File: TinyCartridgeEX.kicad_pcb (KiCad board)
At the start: 2 copper layers, 61.5 x 84.3 mm, 21 parts, among them U1 SN74AVC8T245PW, U2 SN74AVC8T245PW, U3 SN74AVC8T245PW, U4 74AHCV17A, U5 74LVC06A, U6 74LVC1G06, U7 74LVC3G17, U8 74LVC2G132, U9 TinyFPGA_EX, X1 EXPANSION_PORT_C64_EDGE

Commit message: Remove superfluous Schmitt buffers on NAND inputs
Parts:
- removed U8: 74LVC2G132, Package_SO:VSSOP-8_2.4x2.1mm_P0.5mm
- U7: value 74LVC3G17 -> 74LVC2G132; footprint Package_SO:TSSOP-8_3x3mm_P0.65mm -> Package_SO:VSSOP-8_2.4x2.1mm_P0.5mm
- moved U7 5.34 mm to (64.0, 136.4), turned to 0 degrees
- moved R4 4.21 mm to (47.0, 130.7)
- moved R5 4.21 mm to (48.3, 130.7)
- moved R6 4.21 mm to (49.5, 130.7)
- moved R7 4.21 mm to (50.8, 130.7)
- moved R8 4.21 mm to (52.1, 130.7)
- moved R9 4.21 mm to (53.3, 130.7)
- moved C1 3.00 mm to (51.3, 148.5), turned to 180 degrees
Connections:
- U4 pad 10: ~IO2 -> PHI2
- U4 pad 12: ~ROML -> DOTCLK
- U4 pad 3: Net-(U4-Pad3) -> (no net)
- U4 pad 4: PHI2 -> (no net)
- U4 pad 6: ~ROMH -> RESET_IN
- U4 pad 8: ~IO1 -> RW_IN
- U5 pad 2: Net-(U5-Pad2) -> Net-(U4-Pad9)
- U5 pad 6: Net-(U5-Pad6) -> Net-(U4-Pad5)
- U7 pad 1: Net-(U5-Pad2) -> Net-(U7-Pad1)
- U7 pad 2: RESET_IN -> Net-(U7-Pad2)
- U7 pad 3: Net-(U7-Pad3) -> IO12
- U7 pad 5: DOTCLK -> Net-(U7-Pad5)
- U7 pad 6: Net-(U5-Pad6) -> Net-(U7-Pad6)
- U7 pad 7: RW_IN -> ROMLH
- U9 pad 19: PHI2 -> BA
- U9 pad 20: Net-(U8-Pad7) -> IO12
- U9 pad 21: RW_IN -> PHI2
- U9 pad 28: RESET_IN -> RW_IN
- U9 pad 30: Net-(U8-Pad3) -> RESET_IN
- U9 pad 31: BA -> ROMLH
- X1 pad 10: Net-(U4-Pad11) -> Net-(U7-Pad6)
- X1 pad 11: Net-(U4-Pad13) -> Net-(U7-Pad1)
- X1 pad 5: Net-(U5-Pad2) -> Net-(U4-Pad9)
- X1 pad 6: Net-(U7-Pad3) -> Net-(U4-Pad13)
- X1 pad 7: Net-(U4-Pad9) -> Net-(U7-Pad5)
- X1 pad B: Net-(U4-Pad5) -> Net-(U7-Pad2)
- X1 pad C: Net-(U5-Pad6) -> Net-(U4-Pad5)
- X1 pad E: Net-(U4-Pad3) -> Net-(U4-Pad11)
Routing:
- net IO12: track 0.00 -> 43.1 mm
- net Net-(U8-Pad7): track 37.2 -> 0.00 mm
- net Net-(U7-Pad1): track 0.00 -> 35.8 mm, vias 0 -> 2
- net Net-(U7-Pad2): track 0.00 -> 33.5 mm, vias 0 -> 1
- net Net-(U5-Pad6): track 33.2 -> 0.00 mm, vias 3 -> 0
- net Net-(U5-Pad2): track 28.0 -> 0.00 mm
- net ROMLH: track 0.00 -> 27.7 mm
- net Net-(U7-Pad6): track 0.00 -> 26.9 mm
- net Net-(U7-Pad3): track 25.2 -> 0.00 mm
- net Net-(U7-Pad5): track 0.00 -> 25.0 mm
- net Net-(U4-Pad3): track 24.0 -> 0.00 mm, vias 1 -> 0
- net Net-(U8-Pad3): track 22.5 -> 0.00 mm
- net ~ROML: track 21.5 -> 0.00 mm, vias 1 -> 0
- net ~IO1: track 17.7 -> 0.00 mm, vias 1 -> 0
- net ~IO2: track 17.6 -> 0.00 mm, vias 1 -> 0
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
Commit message: Set correct logic families and add Mouser part# and pricing for BOM
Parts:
- U1, U2, U3: value SN74AVC8T245PW -> SN74LVC8T245
- U4: value 74AHCV17A -> 74LV17A
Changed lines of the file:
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@@
       (effects (font (size 1 1) (thickness 0.15)))
     )
-    (fp_text value 74AHCV17A (at 0 3.55 90) (layer F.Fab)
+    (fp_text value 74LV17A (at 0 3.55 90) (layer F.Fab)
       (effects (font (size 1 1) (thickness 0.15)))
     )
@@
       (effects (font (size 1 1) (thickness 0.15)))
     )
-    (fp_text value SN74AVC8T245PW (at 0 4.95 90) (layer F.Fab)
+    (fp_text value SN74LVC8T245 (at 0 4.95 90) (layer F.Fab)
       (effects (font (size 1 1) (thickness 0.15)))
     )
@@
       (effects (font (size 1 1) (thickness 0.15)))
     )
-    (fp_text value SN74AVC8T245PW (at 0 4.95 90) (layer F.Fab)
+    (fp_text value SN74LVC8T245 (at 0 4.95 90) (layer F.Fab)
       (effects (font (size 1 1) (thickness 0.15)))
     )
@@
       (effects (font (size 1 1) (thickness 0.15)))
     )
-    (fp_text value SN74AVC8T245PW (at 0 4.95 90) (layer F.Fab)
+    (fp_text value SN74LVC8T245 (at 0 4.95 90) (layer F.Fab)
       (effects (font (size 1 1) (thickness 0.15)))
     )
@@
   (segment (start 59.055 134.112) (end 55.88 130.937) (width 0.25) (layer F.Cu) (net 42))
   (segment (start 55.88 130.937) (end 55.88 108.839) (width 0.25) (layer F.Cu) (net 42))
+  (segment (start 77.47 153.543) (end 77.47 160.3248) (width 0.25) (layer F.Cu) (net 43))
+  (segment (start 70.428468 149.733) (end 73.66 149.733) (width 0.25) (layer F.Cu) (net 43))
+  (segment (start 73.66 149.733) (end 77.47 153.543) (width 0.25) (layer F.Cu) (net 43))
+  (segment (start 70.428468 149.733) (end 69.469 148.773532) (width 0.25) (layer F.Cu) (net 43))
+  (segment (start 65.958 140.306) (end 65.958 141.814) (width 0.25) (layer F.Cu) (net 43))
+  (via (at 65.958 141.814) (size 0.8) (drill 0.4) (layers F.Cu B.Cu) (net 43))
+  (via (at 69.469 143.764) (size 0.8) (drill 0.4) (layers F.Cu B.Cu) (net 43))
+  (segment (start 69.469 148.773532) (end 69.469 143.764) (width 0.25) (layer F.Cu) (net 43))
+  (segment (start 69.469 143.764) (end 69.469 142.494) (width 0.25) (layer B.Cu) (net 43))
+  (segment (start 68.789 141.814) (end 65.958 141.814) (width 0.25) (layer B.Cu) (net 43))
+  (segment (start 69.469 142.494) (end 68.789 141.814) (width 0.25) (layer B.Cu) (net 43))
+  (segment (start 57.15 151.384) (end 57.15 160.3248) (width 0.25) (layer B.Cu) (net 44))
+  (segment (start 57.15 151.384) (end 57.15 151.257) (width 0.25) (layer B.Cu) (net 44))
+  (segment (start 57.15 151.257) (end 56.388 150.495) (width 0.25) (layer B.Cu) (net 44))
+  (segment (start 56.388 150.495) (end 56.388 143.764) (width 0.25) (layer B.Cu) (net 44))
+  (via (at 56.388 143.764) (size 0.8) (drill 0.4) (layers F.Cu B.Cu) (net 44))
+  (segment (start 55.372 140.306) (end 55.372 141.605) (width 0.25) (layer F.Cu) (net 44))
+  (segment (start 56.388 142.621) (end 56.388 143.764) (width 0.25) (layer F.Cu) (net 44))
+  (segment (start 55.372 141.605) (end 56.388 142.621) (width 0.25) (layer F.Cu) (net 44))
   (segment (start 79.502 134.79) (end 79.502 132.588) (width 0.25) (layer F.Cu) (net 45))
   (via (at 79.502 130.556) (size 0.8) (drill 0.4) (layers F.Cu B.Cu) (net 45))
@@
   (segment (start 82.423 118.237) (end 78.74 114.554) (width 0.25) (layer B.Cu) (net 45))
   (segment (start 78.74 114.554) (end 78.74 101.727) (width 0.25) (layer B.Cu) (net 45))
+  (segment (start 59.69 128.651) (end 59.69 112.141) (width 0.25) (layer F.Cu) (net 46))
+  (segment (start 64.008 132.969) (end 59.69 128.651) (width 0.25) (layer F.Cu) (net 46))
+  (segment (start 64.008 138.031) (end 64.008 132.969) (width 0.25) (layer F.Cu) (net 46))
+  (segment (start 62.708 140.306) (end 62.708 139.331) (width 0.25) (layer F.Cu) (net 46))
+  (segment (start 62.708 139.331) (end 64.008 138.031) (width 0.25) (layer F.Cu) (net 46))
+  (segment (start 59.69 105.283) (end 59.69 96.901) (width 0.25) (layer F.Cu) (net 47))
+  (segment (start 65.308 138.841) (end 64.643 138.176) (width 0.25) (layer F.Cu) (net 47))
+  (segment (start 65.308 140.306) (end 65.308 138.841) (width 0.25) (layer F.Cu) (net 47))
+  (segment (start 64.643 138.176) (end 64.643 131.826) (width 0.25) (layer F.Cu) (net 47))
+  (segment (start 64.643 131.826) (end 60.96 128.143) (width 0.25) (layer F.Cu) (net 47))
+  (segment (start 60.96 106.553) (end 59.69 105.283) (width 0.25) (layer F.Cu) (net 47))
+  (segment (start 60.96 128.143) (end 60.96 106.553) (width 0.25) (layer F.Cu) (net 47))
   (segment (start 100.33 160.3248) (end 100.33 155.448) (width 0.25) (layer F.Cu) (net 48))
   (segment (start 96.266 151.384) (end 88.907 151.384) (width 0.25) (layer F.Cu) (net 48))
@@
   (segment (start 81.911 154.555) (end 81.911 145.852) (width 0.25) (layer F.Cu) (net 55))
   (segment (start 82.55 155.194) (end 81.911 154.555) (width 0.25) (layer F.Cu) (net 55))
-  (segment (start 77.47 153.543) (end 77.47 160.3248) (width 0.25) (layer F.Cu) (net 43))
-  (segment (start 70.428468 149.733) (end 73.66 149.733) (width 0.25) (layer F.Cu) (net 43))
-  (segment (start 73.66 149.733) (end 77.47 153.543) (width 0.25) (layer F.Cu) (net 43))
-  (segment (start 70.428468 149.733) (end 69.469 148.773532) (width 0.25) (layer F.Cu) (net 43))
-  (segment (start 65.958 140.306) (end 65.958 141.814) (width 0.25) (layer F.Cu) (net 43))
-  (via (at 65.958 141.814) (size 0.8) (drill 0.4) (layers F.Cu B.Cu) (net 43))
-  (via (at 69.469 143.764) (size 0.8) (drill 0.4) (layers F.Cu B.Cu) (net 43))
-  (segment (start 69.469 148.773532) (end 69.469 143.764) (width 0.25) (layer F.Cu) (net 43))
-  (segment (start 69.469 143.764) (end 69.469 142.494) (width 0.25) (layer B.Cu) (net 43))
-  (segment (start 68.789 141.814) (end 65.958 141.814) (width 0.25) (layer B.Cu) (net 43))
-  (segment (start 69.469 142.494) (end 68.789 141.814) (width 0.25) (layer B.Cu) (net 43))
-  (segment (start 57.15 151.384) (end 57.15 160.3248) (width 0.25) (layer B.Cu) (net 44))
-  (segment (start 57.15 151.384) (end 57.15 151.257) (width 0.25) (layer B.Cu) (net 44))
-  (segment (start 57.15 151.257) (end 56.388 150.495) (width 0.25) (layer B.Cu) (net 44))
-  (segment (start 56.388 150.495) (end 56.388 143.764) (width 0.25) (layer B.Cu) (net 44))
-  (via (at 56.388 143.764) (size 0.8) (drill 0.4) (layers F.Cu B.Cu) (net 44))
-  (segment (start 55.372 140.306) (end 55.372 141.605) (width 0.25) (layer F.Cu) (net 44))
-  (segment (start 56.388 142.621) (end 56.388 143.764) (width 0.25) (layer F.Cu) (net 44))
-  (segment (start 55.372 141.605) (end 56.388 142.621) (width 0.25) (layer F.Cu) (net 44))
-  (segment (start 59.69 128.651) (end 59.69 112.141) (width 0.25) (layer F.Cu) (net 46))
-  (segment (start 64.008 132.969) (end 59.69 128.651) (width 0.25) (layer F.Cu) (net 46))
-  (segment (start 64.008 138.031) (end 64.008 132.969) (width 0.25) (layer F.Cu) (net 46))
-  (segment (start 62.708 140.306) (end 62.708 139.331) (width 0.25) (layer F.Cu) (net 46))
-  (segment (start 62.708 139.331) (end 64.008 138.031) (width 0.25) (layer F.Cu) (net 46))
-  (segment (start 59.69 105.283) (end 59.69 96.901) (width 0.25) (layer F.Cu) (net 47))
-  (segment (start 65.308 138.841) (end 64.643 138.176) (width 0.25) (layer F.Cu) (net 47))
-  (segment (start 65.308 140.306) (end 65.308 138.841) (width 0.25) (layer F.Cu) (net 47))
-  (segment (start 64.643 138.176) (end 64.643 131.826) (width 0.25) (layer F.Cu) (net 47))
-  (segment (start 64.643 131.826) (end 60.96 128.143) (width 0.25) (layer F.Cu) (net 47))
-  (segment (start 60.96 106.553) (end 59.69 105.283) (width 0.25) (layer F.Cu) (net 47))
-  (segment (start 60.96 128.143) (end 60.96 106.553) (width 0.25) (layer F.Cu) (net 47))
   (segment (start 62.23 160.3248) (end 62.23 151.892) (width 0.25) (layer F.Cu) (net 56))
   (segment (start 65.308 148.814) (end 65.308 146.206) (width 0.25) (layer F.Cu) (net 56))

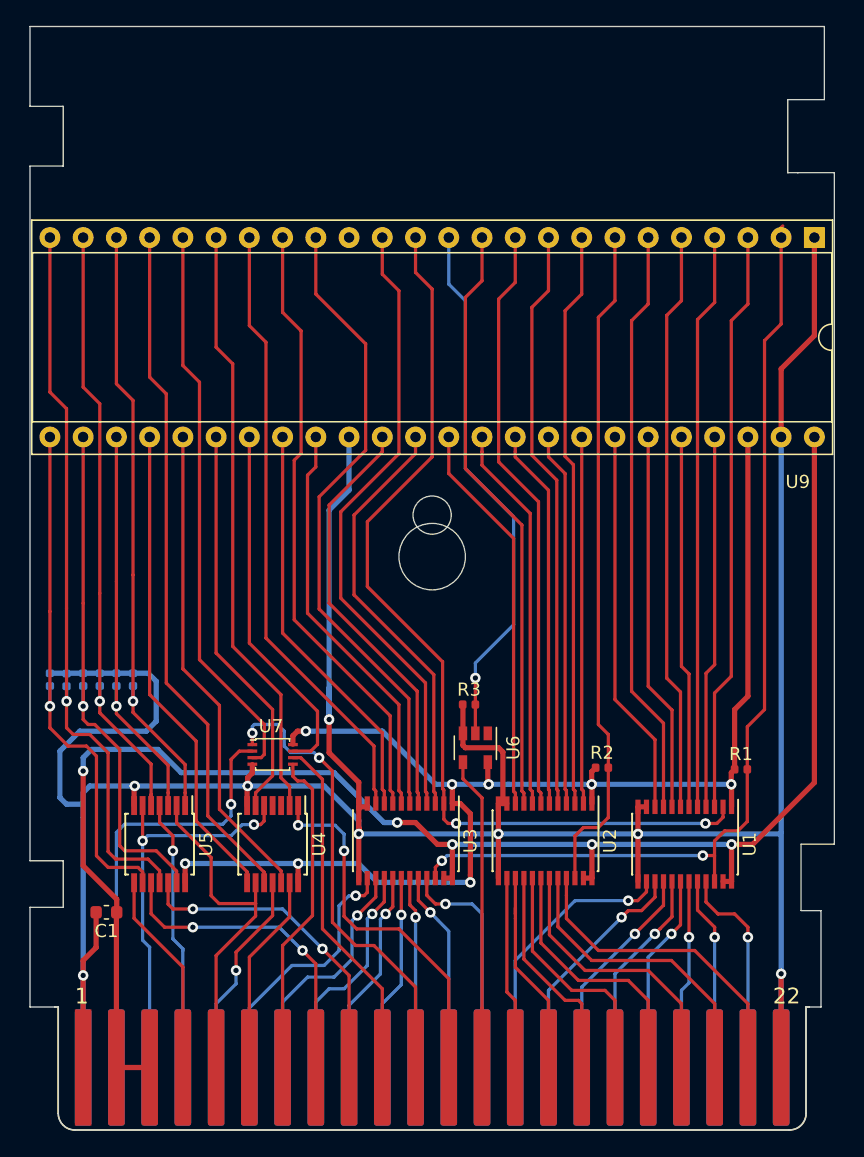
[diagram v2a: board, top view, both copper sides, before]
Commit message: Fix PCB outline and add some logos/text
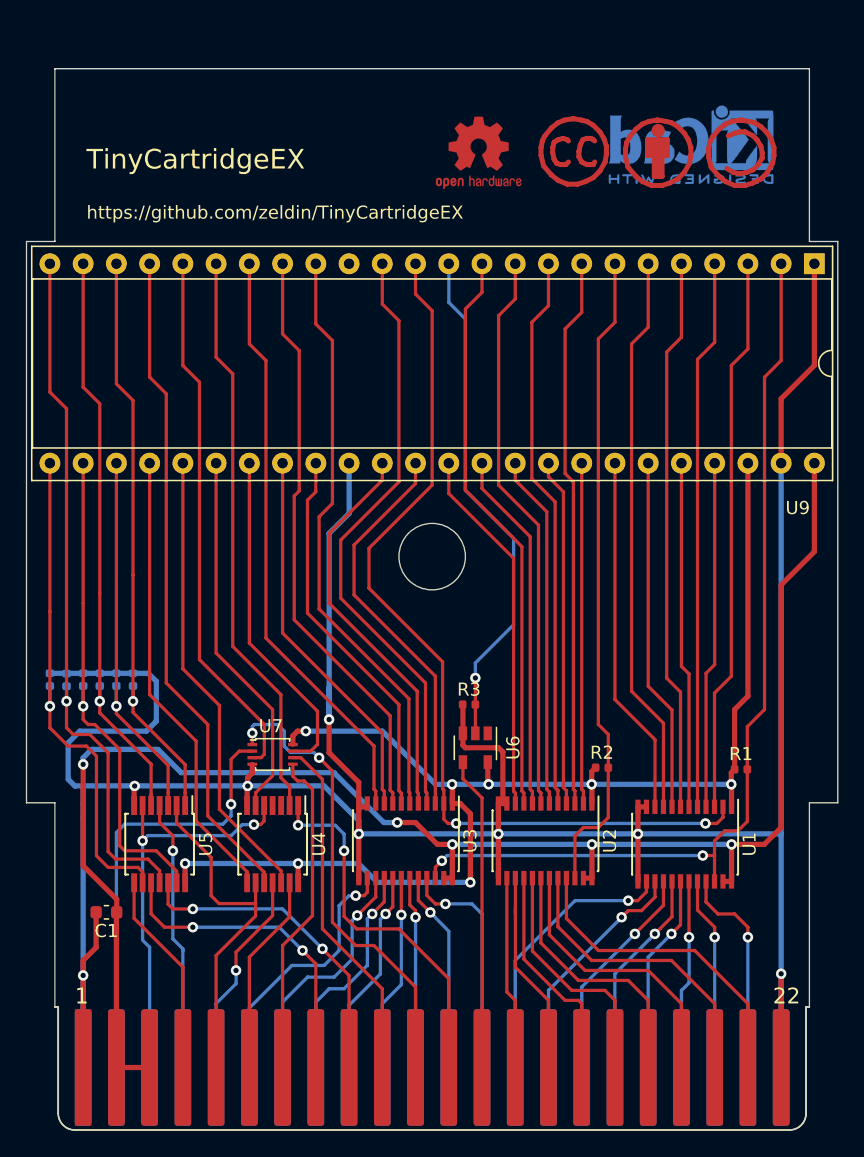
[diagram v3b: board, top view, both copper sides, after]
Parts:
- added REFBY: Symbol_CC-Attribution_CopperTop_Small, Symbol:Symbol_CC-Attribution_CopperTop_Small, F.Cu at (93.5, 90.4)
- added REFCC: Symbol_CreativeCommons_CopperTop_Type2_Small, Symbol:Symbol_CreativeCommons_CopperTop_Type2_Small, F.Cu at (86.9, 90.4)
- added REFKI: KiCad-Logo2_5mm_Copper, Symbol:KiCad-Logo2_5mm_Copper, B.Cu at (96.0, 89.8)
- added REFOSHW: OSHW-Logo2_7.3x6mm_Copper, Symbol:OSHW-Logo2_7.3x6mm_Copper, F.Cu at (79.8, 90.4)
- added REFSA: Symbol_CC-ShareAlike_CopperTop_Small, Symbol:Symbol_CC-ShareAlike_CopperTop_Small, F.Cu at (99.8, 90.4)
- moved U9 2.00 mm to (105.4, 98.9)
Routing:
- net GND: track 253.1 -> 247.0 mm
- net A11: track 49.2 -> 45.1 mm
- net A_~EN: track 75.4 -> 72.5 mm
- net A13: track 47.2 -> 45.1 mm
- net A_DIR: track 71.9 -> 69.8 mm
- net VCC: track 103.1 -> 101.1 mm
- net D4: track 45.1 -> 43.1 mm
- net DOTCLK: track 37.2 -> 35.2 mm
- net DMA: track 41.2 -> 39.2 mm
- net D1: track 28.6 -> 26.6 mm
- net A9: track 48.3 -> 46.3 mm
- net A12: track 31.2 -> 29.2 mm
- net D3: track 29.1 -> 27.1 mm
- net A8: track 32.5 -> 30.5 mm
- net A3: track 28.5 -> 26.5 mm
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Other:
- board size 61.5 x 84.3 mm -> 62 x 81.1 mm
- board text added: "TinyCartridgeEX"
- board text added: "https://github.com/zeldin/TinyCartridgeEX"
